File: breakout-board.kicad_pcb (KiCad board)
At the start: 2 copper layers, 81 x 47 mm, 19 parts, among them J1 Conn_01x04_Male, J10 Conn_01x02_Male, J2 Conn_01x08_Male, J3 Conn_01x08_Male, J4 Conn_01x02_Male, J5 Conn_02x08_Counter_Clockwise, J6 Conn_01x08_Male, J7 Conn_01x02_Male, J8 Conn_01x02_Male, J9 Conn_01x02_Male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

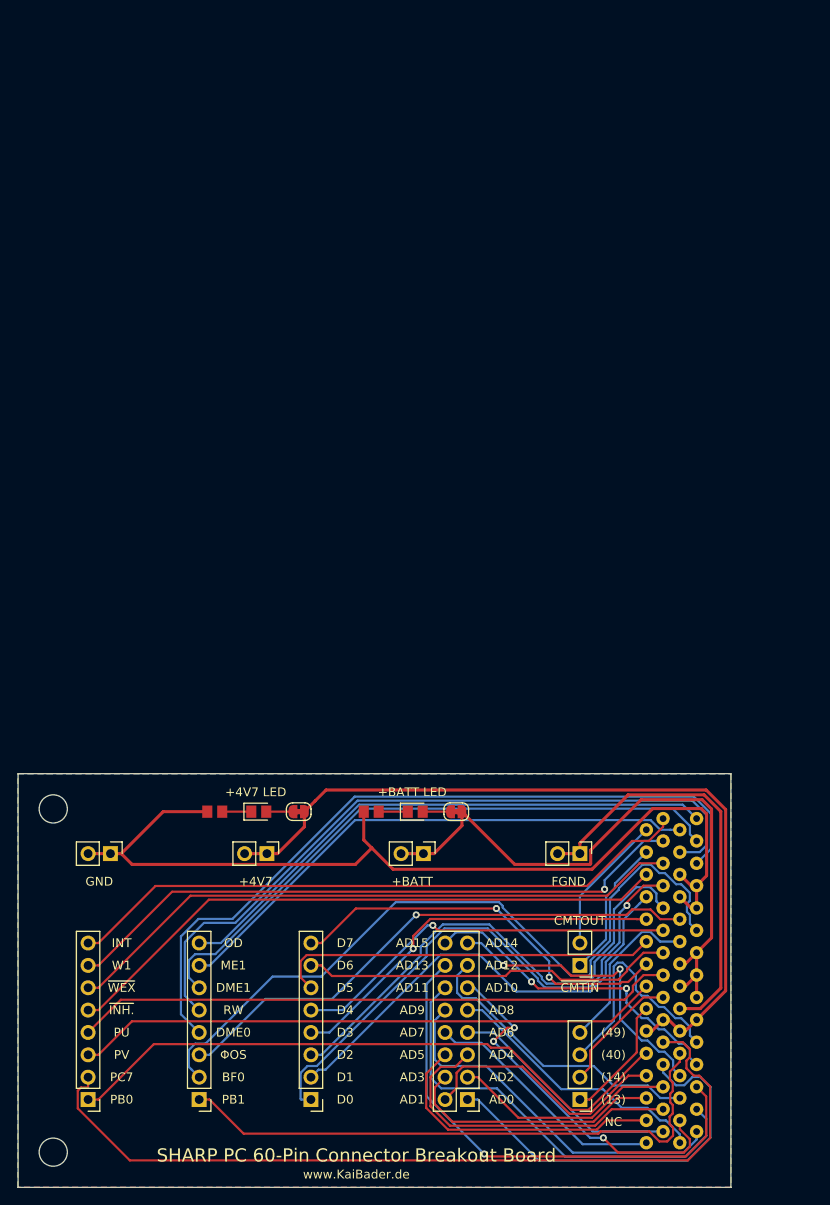
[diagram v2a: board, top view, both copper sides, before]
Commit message: Rev. 1.0 of the Sharp PC-1500 60-Pin Connector Breakout Board.
Squashed commit of various design updates.
Fixed one falsely documented FGND pin.
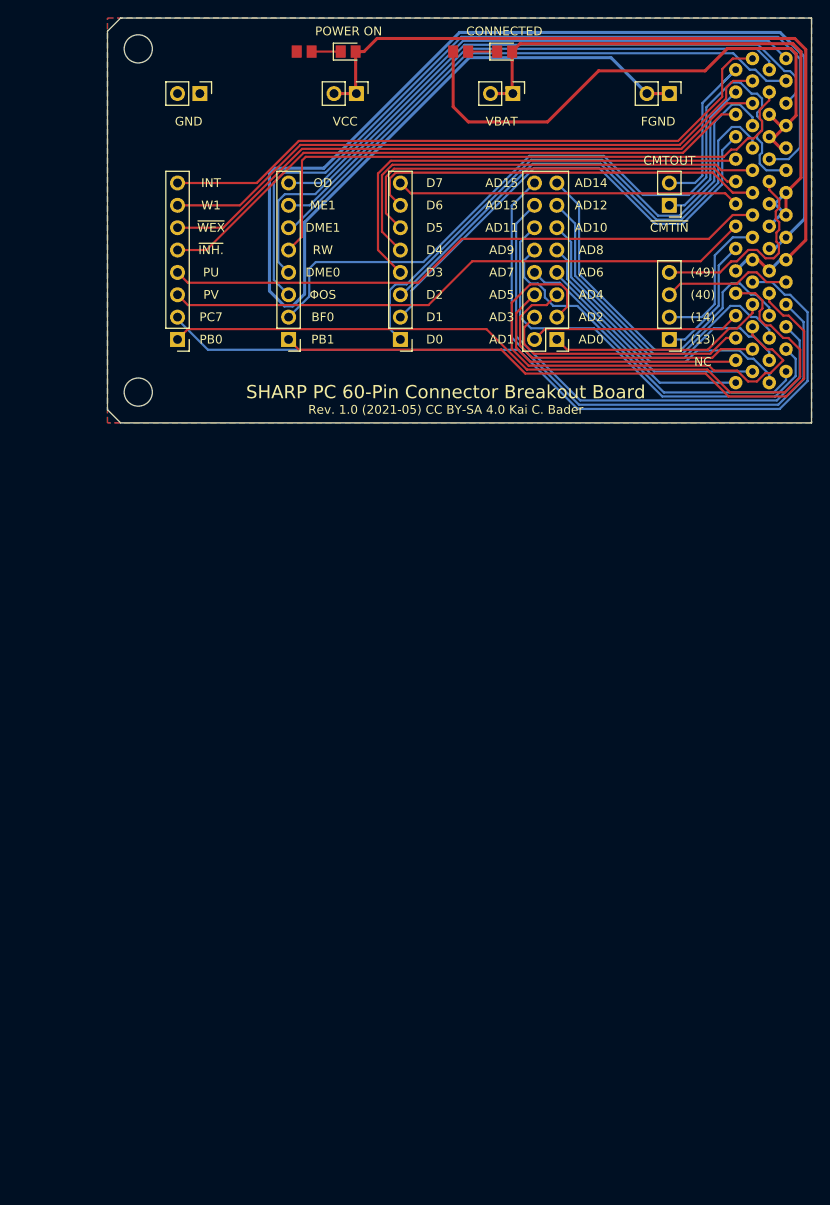
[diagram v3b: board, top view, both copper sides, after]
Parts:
- removed JP1, JP2: SolderJumper_2_Bridged, Jumper:SolderJumper-2_P1.3mm_Bridged_RoundedPad1.0x1.5mm
- removed REF1, REF2: MountingHole_3.2mm_M3, MountingHole:MountingHole_3.2mm_M3
- added H1: M3, MountingHole:MountingHole_3.2mm_M3, F.Cu at (66.7, 40.6)
- added H2: M3, MountingHole:MountingHole_3.2mm_M3, F.Cu at (66.7, 79.6)
- D1: value LED -> 4V7
- D2: value LED -> BATT
- J1: value Conn_01x04_Male -> NC
- J10: value Conn_01x02_Male -> GND
- J2: value Conn_01x08_Male -> PINS1
- J3: value Conn_01x08_Male -> PINS2
- J4: value Conn_01x02_Male -> CMT
- J5: value Conn_02x08_Counter_Clockwise -> A-BUS
- J6: value Conn_01x08_Male -> D-BUS
- J7: value Conn_01x02_Male -> FGND
- J8: value Conn_01x02_Male -> 4V7
- J9: value Conn_01x02_Male -> BATT
- P1: value Sharp_Connector_60 -> 60-Pin Connector
- R1: value R -> 470
- R2: value R -> 1.2k
- moved J1 87.0 mm to (127.0, 73.7)
- moved J10 87.0 mm to (73.7, 45.7)
- moved J2 87.0 mm to (71.1, 73.7)
- moved J3 87.0 mm to (83.7, 73.7)
- moved J5 87.0 mm to (114.2, 73.7)
- moved J6 87.0 mm to (96.4, 73.7)
- moved J7 87.0 mm to (127.0, 45.7)
- moved J8 87.0 mm to (91.4, 45.7)
- moved J9 87.0 mm to (109.2, 45.7)
- moved D1 87.0 mm to (90.5, 41.0)
- moved D2 87.0 mm to (108.3, 41.0)
- moved J4 87.0 mm to (127.0, 58.4)
- moved R1 87.0 mm to (85.5, 41.0)
- moved R2 87.0 mm to (103.3, 41.0)
- moved P1 87.0 mm to (137.7, 59.5)
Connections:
- D1 pad 2: Net-(D1-Pad2) -> +4V7
- D2 pad 2: Net-(D2-Pad2) -> +BATT
- P1 pad 44: +BATT -> /FGND
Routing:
- net /FGND: track 48.5 -> 170.6 mm
- net GND: track 108.0 -> 65.6 mm
- net /ΦOS: track 61.9 -> 95.2 mm, vias 1 -> 0
- net /AD2: track 25.6 -> 55.2 mm
- net /AD15: track 36.8 -> 65.5 mm, vias 2 -> 0
- net /AD0: track 45.1 -> 25.4 mm
- net /PB0: track 71.8 -> 89.7 mm
- net /RW: track 81.8 -> 69.4 mm
- net /NC3: track 27.1 -> 14.8 mm
- net /D3: track 44.3 -> 53.6 mm, vias 1 -> 0
- net /D4: track 44.2 -> 52.2 mm, vias 1 -> 0
- net /AD14: track 34.9 -> 42.8 mm, vias 2 -> 0
- net /PB1: track 66.8 -> 73.8 mm
- net /D7: track 45.3 -> 39.1 mm, vias 2 -> 0
- net /DME0: track 85.7 -> 79.7 mm
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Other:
- board size 81 x 47 mm -> 80 x 46 mm
- net class PWR added: clearance 0.2, trace_width 0.35, via_dia 0.8, via_drill 0.4
- net class pwr removed
- board text added: "CONNECTED"
- board text added: "POWER ON"
- board text added: "Rev. 1.0 (2021-05) CC BY-SA 4.0 Kai C. Bader"
- board text added: "VBAT"
- board text added: "VCC"
- board text removed: "+4V7"
- board text removed: "+4V7 LED"
- board text removed: "+BATT"
- board text removed: "+BATT LED"
- board text removed: "www.KaiBader.de"
